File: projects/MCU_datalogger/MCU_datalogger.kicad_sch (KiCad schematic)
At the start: 0 parts

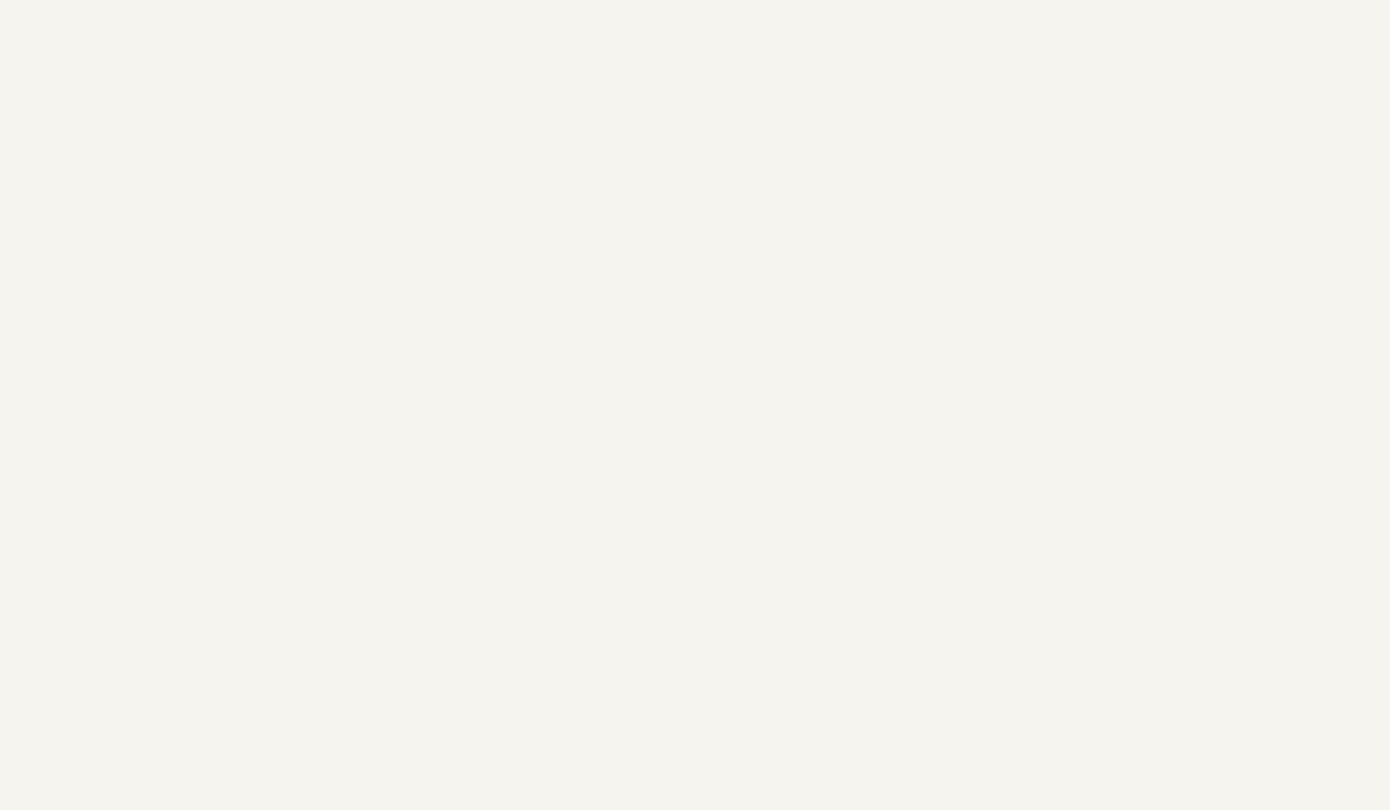
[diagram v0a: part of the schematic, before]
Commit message: Add components to MCU dataloogger
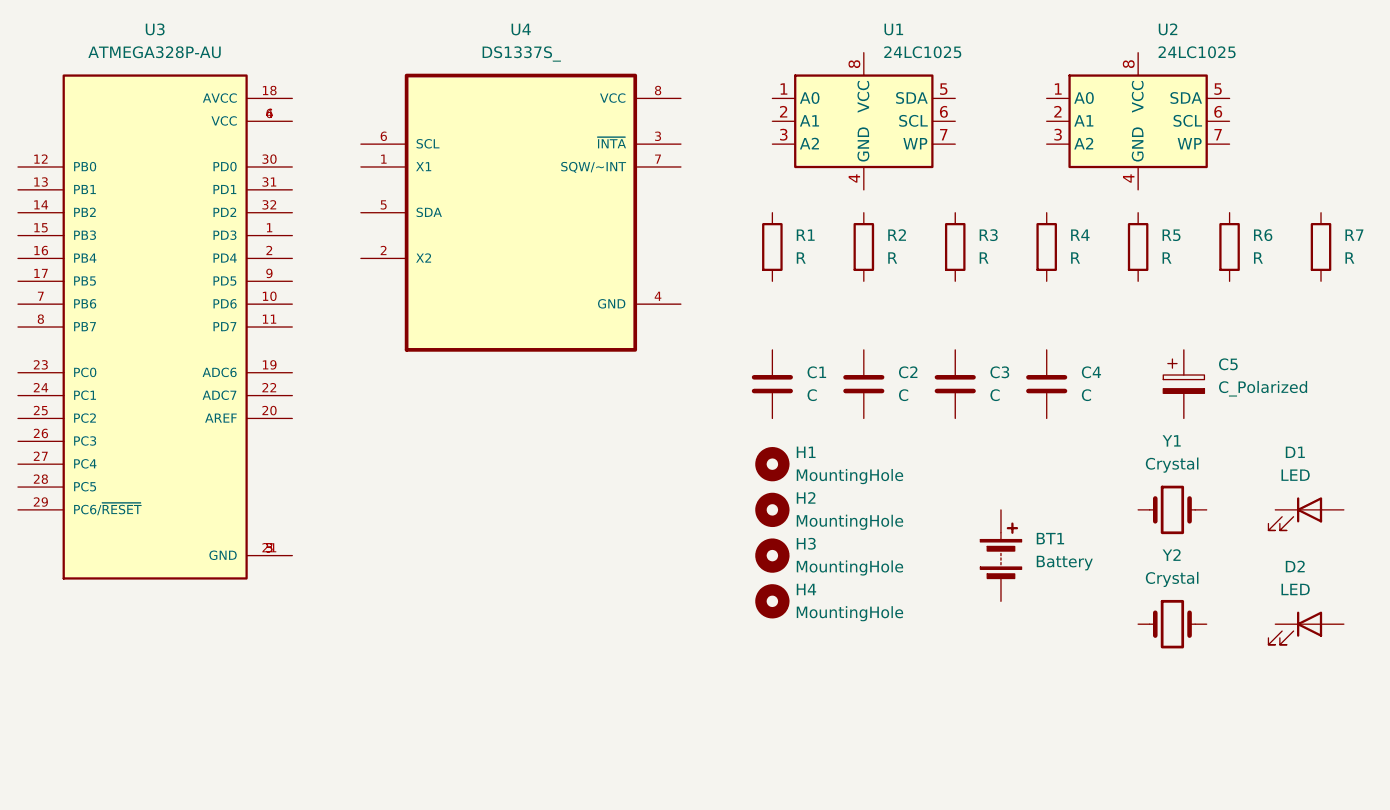
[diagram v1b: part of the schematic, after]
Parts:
- added BT1: Battery, symbol Device:Battery
- added C1, C2, C3, C4: C, symbol Device:C
- added C5: C_Polarized, symbol Device:C_Polarized
- added D1, D2: LED, symbol Device:LED
- added H1, H2, H3, H4: MountingHole, symbol Mechanical:MountingHole
- added R1, R2, R3, R4, R5, R6, R7: R, symbol Device:R
- added U1, U2: 24LC1025, symbol Memory_EEPROM:24LC1025
- added U3: ATMEGA328P-AU, ATMEGA328P-AU:QFP80P900X900X120-32N, symbol MH_ATMEGA328:ATMEGA328P-AU
- added U4: DS1337S_, DS1337S_:SOIC127P600X175-8N, symbol MH_DS13375:DS1337S_
- added Y1, Y2: Crystal, symbol Device:Crystal
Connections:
- new net: U3.21 (GND), U3.3 (GND), U3.5 (GND)
- new net: U3.4 (VCC), U3.6 (VCC)

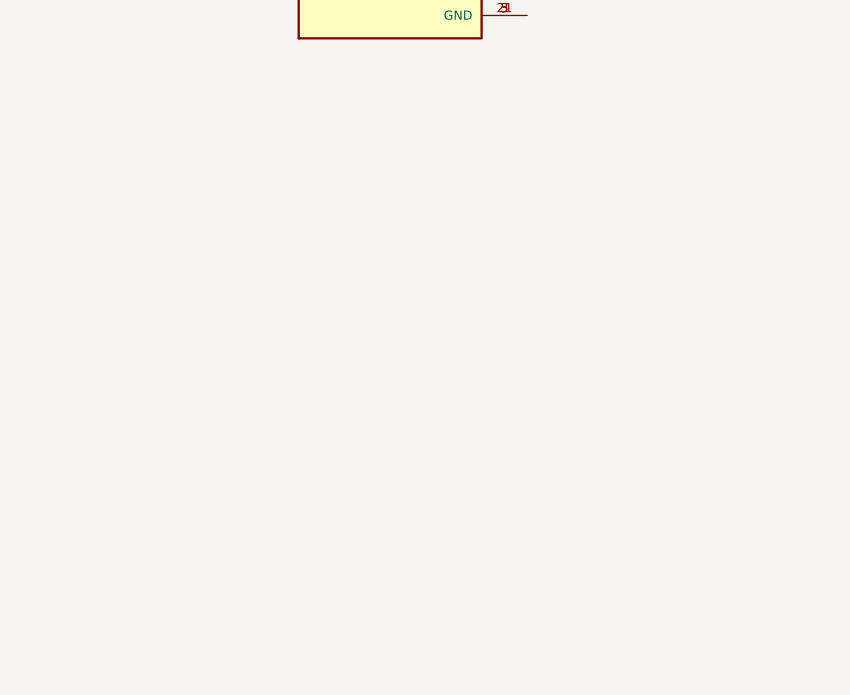
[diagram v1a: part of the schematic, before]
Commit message: In MCU datalogger project add sheet 'Connectors'
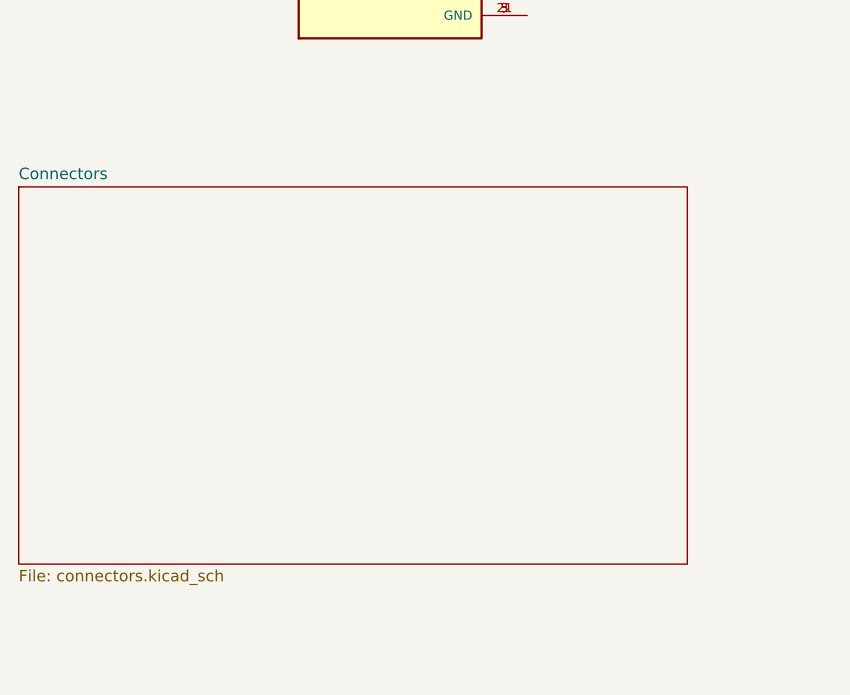
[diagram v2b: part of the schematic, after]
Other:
- added sheet Connectors (connectors.kicad_sch)
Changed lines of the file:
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@@
 	(title_block
 		(title "MCU datalogger")
-		(date "2025-09-29")
+		(date "2025-12-24")
 		(rev "0.1")
 		(company "Manuel Heredia - sevillabot")
@@
 				)
 			)
+		)
+	)
+	(sheet
+		(at 52.705 143.51)
+		(size 74.295 41.91)
+		(exclude_from_sim no)
+		(in_bom yes)
+		(on_board yes)
+		(dnp no)
+		(fields_autoplaced yes)
+		(stroke
+			(width 0.1524)
+			(type solid)
+		)
+		(fill
+			(color 0 0 0 0.0000)
+		)
+		(property "Sheetname" "Connectors"
+			(at 52.705 142.7984 0)
+			(effects
+				(font
+					(size 1.27 1.27)
+				)
+				(justify left bottom)
+			)
+		)
+		(property "Sheetfile" "connectors.kicad_sch"
+			(at 52.705 186.0046 0)
+			(effects
+				(font
+					(size 1.27 1.27)
+				)
+				(justify left top)
+			)
+		)
+		(instances
+			(project "MCU_datalogger"
+				(path "/7bf4f70a-c379-4f6a-bba1-afc53ccea3c5"
+					(page "2")
+				)
+			)

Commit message: MC_datalogger - Arrange and anotate symbols
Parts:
- renumbered C3 to C1, C1 to C3, D2 to D1, D1 to D2, R5 to R1, R4 to R3, R3 to R4, R6 to R5, R1 to R6, U4 to U2, U2 to U3, U3 to U4
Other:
- moved on the sheet: BT1, C1, C2, C3, C4, C5, D1, D2, H1, H2, H3, H4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

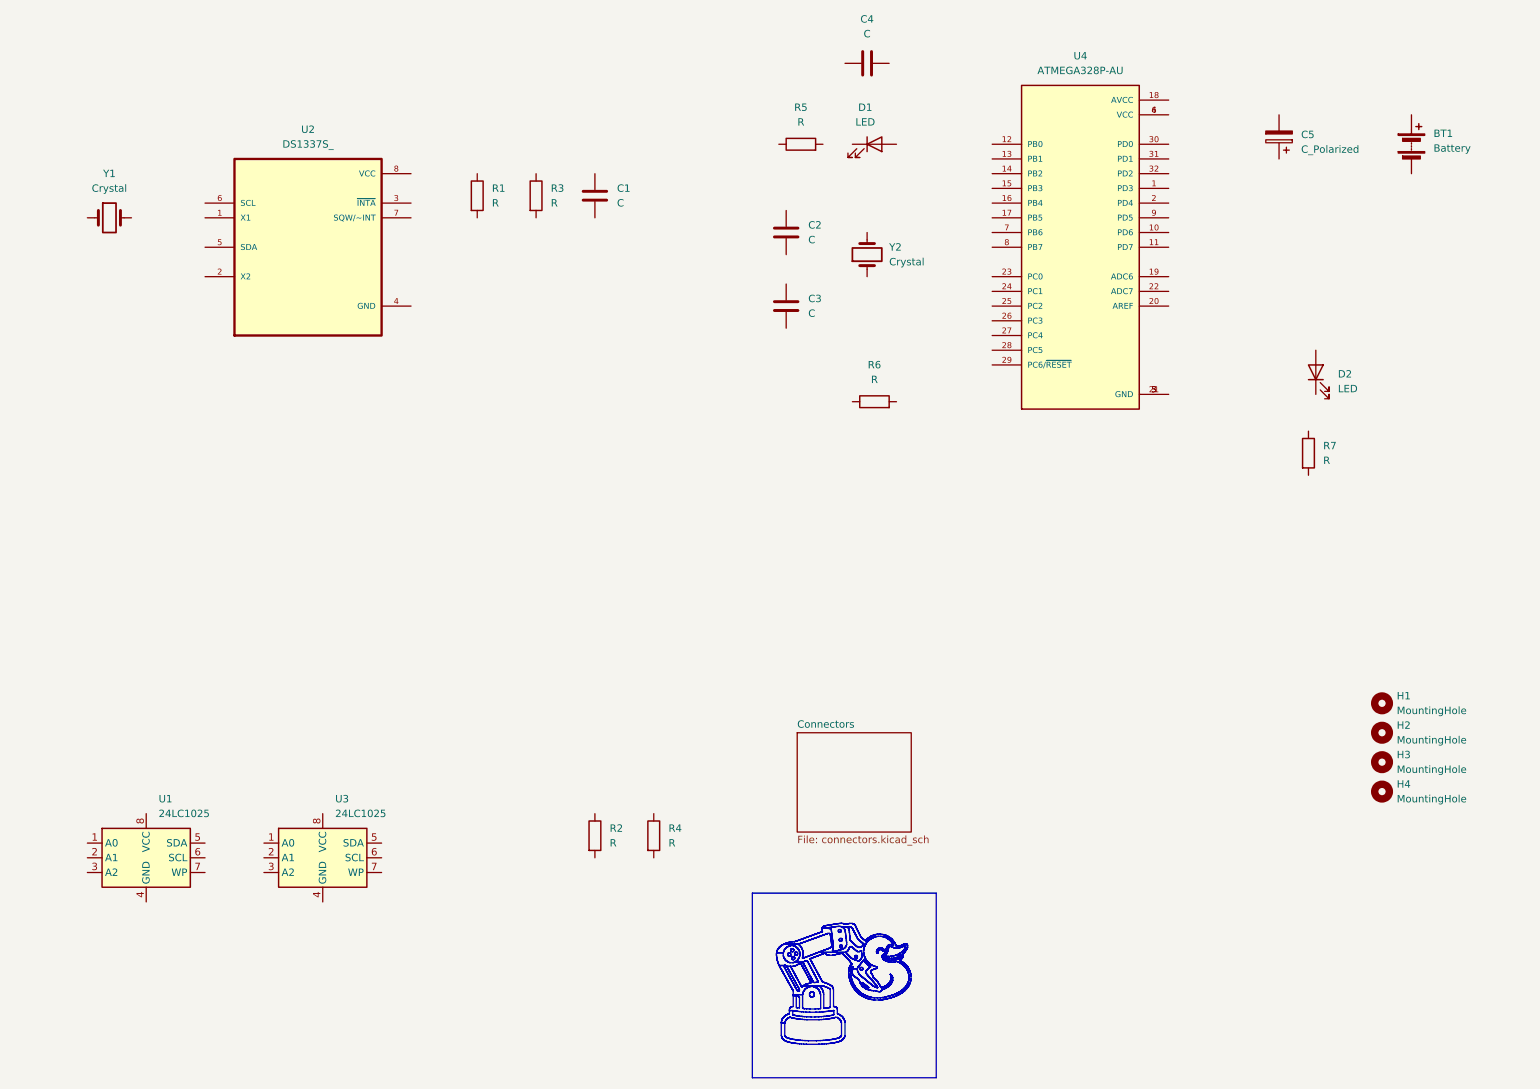
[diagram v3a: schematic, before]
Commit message: MCU datalogger - add component values
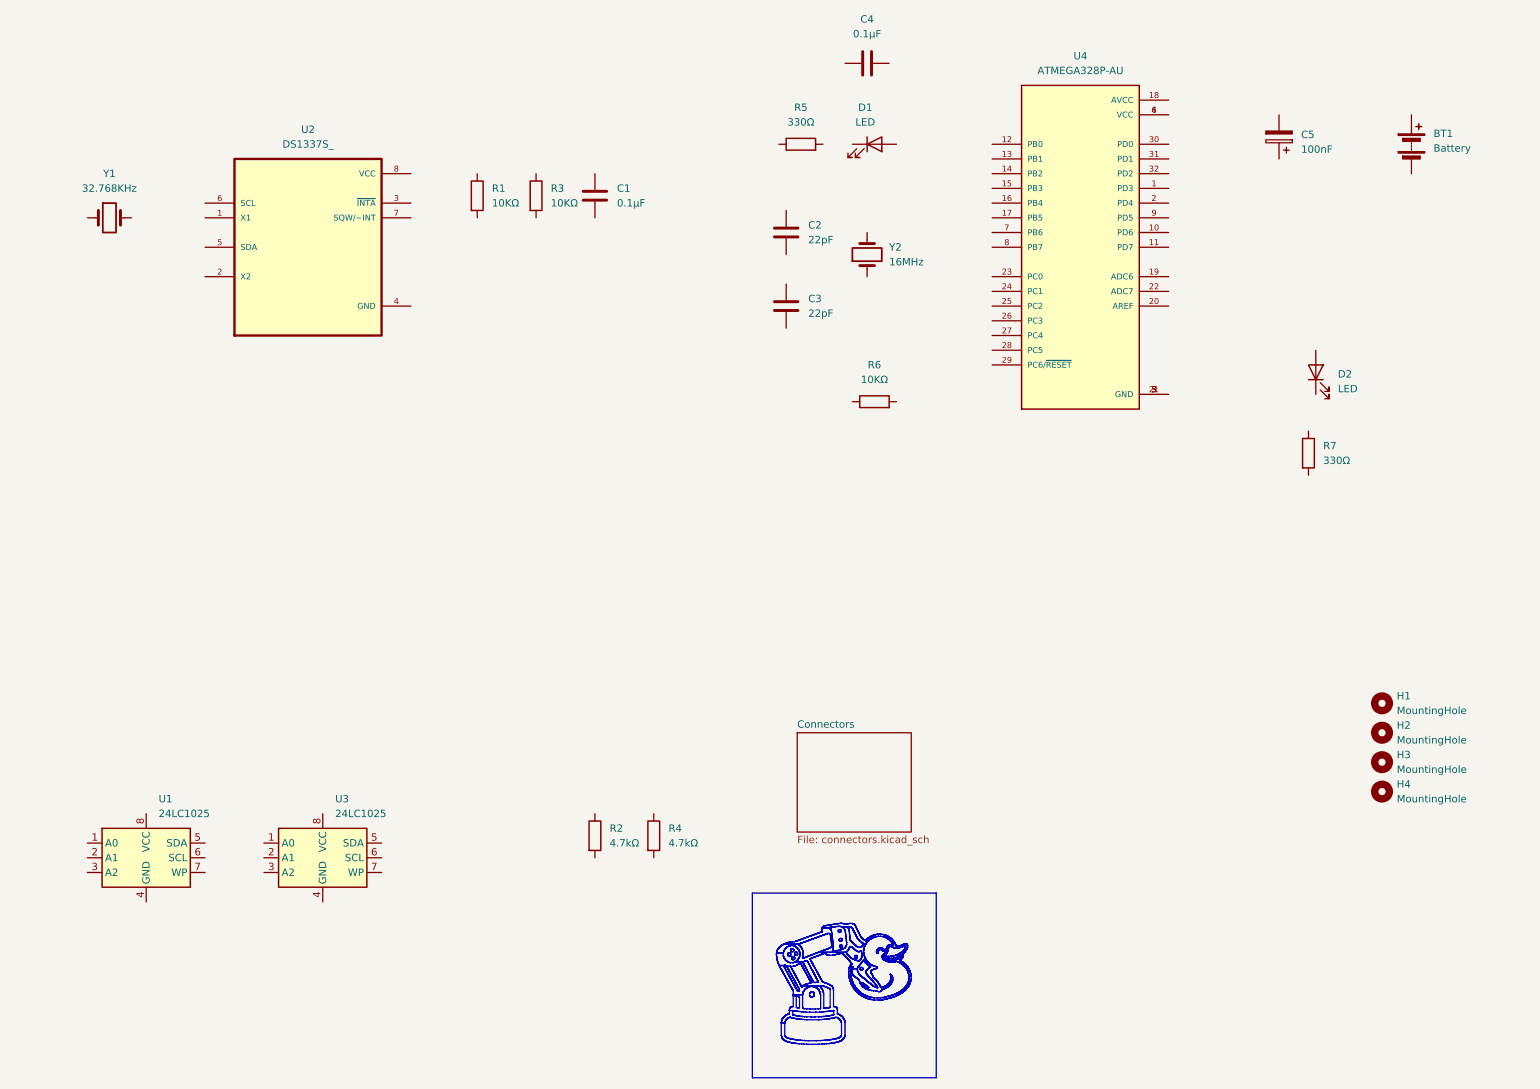
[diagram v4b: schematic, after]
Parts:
- C1, C4: value C -> 0.1μF
- C2, C3: value C -> 22pF
- C5: value C_Polarized -> 100nF
- R1, R3, R6: value R -> 10KΩ
- R2, R4: value R -> 4.7kΩ
- R5, R7: value R -> 330Ω
- Y1: value Crystal -> 32.768KHz
- Y2: value Crystal -> 16MHz

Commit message: MCU datalogger - associate footprints
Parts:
- BT1: footprint (none) -> Connector_PinHeader_2.54mm:PinHeader_1x02_P2.54mm_Vertical
- C1, C2, C3, C4, C5: footprint (none) -> Capacitor_SMD:C_1206_3216Metric_Pad1.33x1.80mm_HandSolder
- D1, D2: footprint (none) -> LED_SMD:LED_1206_3216Metric_Pad1.42x1.75mm_HandSolder
- H1, H2, H3, H4: footprint (none) -> MountingHole:MountingHole_2.2mm_M2
- R1, R2, R3, R4, R5, R6, R7: footprint (none) -> Resistor_SMD:R_1206_3216Metric_Pad1.30x1.75mm_HandSolder
- U1, U3: footprint (none) -> Package_SO:SOIC-8_5.3x5.3mm_P1.27mm
- U2: footprint DS1337S_:SOIC127P600X175-8N -> MH_DS1337S:SOIC127P600X175-8N
- U4: footprint ATMEGA328P-AU:QFP80P900X900X120-32N -> MH_ATMEGA328:QFP80P900X900X120-32N
- Y1: footprint (none) -> Crystal:Crystal_SMD_3215-2Pin_3.2x1.5mm
- Y2: footprint (none) -> Crystal:Crystal_SMD_5032-2Pin_5.0x3.2mm_HandSoldering
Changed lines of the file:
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@@
 			)
 		)
-		(property "Footprint" ""
+		(property "Footprint" "Capacitor_SMD:C_1206_3216Metric_Pad1.33x1.80mm_HandSolder"
 			(at 152.0952 68.58 0)
 			(effects
@@
 			)
 		)
-		(property "Footprint" ""
+		(property "Footprint" "Connector_PinHeader_2.54mm:PinHeader_1x02_P2.54mm_Vertical"
 			(at 259.08 35.306 90)
 			(effects
@@
 			)
 		)
-		(property "Footprint" ""
+		(property "Footprint" "LED_SMD:LED_1206_3216Metric_Pad1.42x1.75mm_HandSolder"
 			(at 242.57 76.2 0)
 			(effects
@@
 			)
 		)
-		(property "Footprint" ""
+		(property "Footprint" "MountingHole:MountingHole_2.2mm_M2"
 			(at 254 143.51 0)
 			(effects
@@
 			)
 		)
-		(property "Footprint" ""
+		(property "Footprint" "MountingHole:MountingHole_2.2mm_M2"
 			(at 254 133.35 0)
 			(effects
@@
 			)
 		)
-		(property "Footprint" ""
+		(property "Footprint" "Resistor_SMD:R_1206_3216Metric_Pad1.30x1.75mm_HandSolder"
 			(at 126.492 156.21 90)
 			(effects
@@
 			)
 		)
-		(property "Footprint" ""
+		(property "Footprint" "Resistor_SMD:R_1206_3216Metric_Pad1.30x1.75mm_HandSolder"
 			(at 153.67 38.608 90)
 			(effects
@@
 			)
 		)
-		(property "Footprint" ""
+		(property "Footprint" "Capacitor_SMD:C_1206_3216Metric_Pad1.33x1.80mm_HandSolder"
 			(at 235.2548 31.75 0)
 			(effects
@@
 			)
 		)
-		(property "Footprint" ""
+		(property "Footprint" "MountingHole:MountingHole_2.2mm_M2"
 			(at 254 138.43 0)
 			(effects
@@
 			)
 		)
-		(property "Footprint" ""
+		(property "Footprint" "Capacitor_SMD:C_1206_3216Metric_Pad1.33x1.80mm_HandSolder"
 			(at 152.0952 55.88 0)
 			(effects
@@
 			)
 		)
-		(property "Footprint" ""
+		(property "Footprint" "LED_SMD:LED_1206_3216Metric_Pad1.42x1.75mm_HandSolder"
 			(at 166.37 36.83 0)
 			(effects
@@
 			)
 		)
-		(property "Footprint" ""
+		(property "Footprint" "Capacitor_SMD:C_1206_3216Metric_Pad1.33x1.80mm_HandSolder"
 			(at 119.0752 49.53 0)
 			(effects
@@
 			)
 		)
-		(property "Footprint" ""
+		(property "Footprint" "Resistor_SMD:R_1206_3216Metric_Pad1.30x1.75mm_HandSolder"
 			(at 106.172 45.72 90)
 			(effects
@@
 			)
 		)
-		(property "Footprint" ""
+		(property "Footprint" "Resistor_SMD:R_1206_3216Metric_Pad1.30x1.75mm_HandSolder"
 			(at 166.37 83.058 90)
 			(effects
@@
 			)
 		)
-		(property "Footprint" ""
+		(property "Footprint" "Resistor_SMD:R_1206_3216Metric_Pad1.30x1.75mm_HandSolder"
 			(at 239.522 90.17 90)
 			(effects
@@
 			)
 		)
-		(property "Footprint" ""
+		(property "Footprint" "Crystal:Crystal_SMD_5032-2Pin_5.0x3.2mm_HandSoldering"
 			(at 165.1 55.88 0)
 			(effects
@@
 			)
 		)
-		(property "Footprint" ""
+		(property "Footprint" "Crystal:Crystal_SMD_3215-2Pin_3.2x1.5mm"
 			(at 34.29 49.53 0)
 			(effects
@@
 			)
 		)
-		(property "Footprint" ""
+		(property "Footprint" "Capacitor_SMD:C_1206_3216Metric_Pad1.33x1.80mm_HandSolder"
 			(at 168.91 21.8948 0)
 			(effects
@@
 			)
 		)
-		(property "Footprint" "DS1337S_:SOIC127P600X175-8N"
+		(property "Footprint" "MH_DS1337S:SOIC127P600X175-8N"
 			(at 68.58 54.61 0)
 			(effects
@@
 			)
 		)
+		(property "MH_Role" ""
+			(at 68.58 54.61 0)
+			(effects
+				(font
+					(size 1.27 1.27)
+				)
+			)
+		)
 		(pin "1"
 		)
@@
 			)
 		)
-		(property "Footprint" "ATMEGA328P-AU:QFP80P900X900X120-32N"
+		(property "Footprint" "MH_ATMEGA328:QFP80P900X900X120-32N"
 			(at 201.93 54.61 0)
 			(effects
@@
 			)
 		)
+		(property "MH_Role" ""
+			(at 201.93 54.61 0)
+			(effects
+				(font
+					(size 1.27 1.27)
+				)
+			)
+		)
 		(pin "8"
 		)
@@
 			)
 		)
-		(property "Footprint" ""
+		(property "Footprint" "Resistor_SMD:R_1206_3216Metric_Pad1.30x1.75mm_HandSolder"
 			(at 96.012 45.72 90)
 			(effects
@@
 			)
 		)
-		(property "Footprint" ""
+		(property "Footprint" "MountingHole:MountingHole_2.2mm_M2"
 			(at 254 148.59 0)
 			(effects
@@
 			)
 		)
-		(property "Footprint" ""
+		(property "Footprint" "Package_SO:SOIC-8_5.3x5.3mm_P1.27mm"
 			(at 71.12 160.02 0)
 			(effects
@@
 			)
 		)
-		(property "Footprint" ""
+		(property "Footprint" "Resistor_SMD:R_1206_3216Metric_Pad1.30x1.75mm_HandSolder"
 			(at 116.332 156.21 90)
 			(effects
@@
 			)
 		)
-		(property "Footprint" ""
+		(property "Footprint" "Package_SO:SOIC-8_5.3x5.3mm_P1.27mm"
 			(at 40.64 160.02 0)
 			(effects
